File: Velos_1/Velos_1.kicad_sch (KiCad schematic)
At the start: 31 parts, among them J1 conector_motor, J2 S_Bus, J3 llave_habilitacion, J4 parada_emergencia, J5 V_in +9VDC, J6 Control Driver, K1 Relay_SPDT, Q1 BC548, Q2 BC548, Q3 BC548, Q4 BC548, Q5 BC548, U1 LM358, U2 L7805

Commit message: nano a mega y cambios en circuito atenuador
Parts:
- removed A1: Arduino_Nano_v2.x, Module:Arduino_Nano, symbol MCU_Module:Arduino_Nano_v2.x
- removed C2: 100nF, symbol Device:C
- removed R5: 33k, Resistor_THT:R_Axial_DIN0204_L3.6mm_D1.6mm_P5.08mm_Horizontal, symbol Device:R
- C1: value 100nF -> 100uF
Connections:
- net Ref vel_0 is gone; now on net Ref vel_D: RV1.2
- net +9V: now also A2.VIN
- net Analog_out: now also RV2.3; no longer RV2.1
- net Dir: now also A2.D5
- net Enable: now also A2.D6
- net GND: now also A2.GND6 (GND), U1.3 (+); no longer RV2.3
- net PWM: now also A2.D7
- net Puls: now also A2.D4
- net S-BUS: now also A2.D9
- net at C1.1, R4.2: now also RV2.1
- net at Q2.1 (C), R3.2: now also A2.D3 (D3_INT1)
- net at R1.2: now also A2.D2 (D2_INT0)
- net Ref vel_D: now reaches A2.A0
- no-connect marks 22 -> 78
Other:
- moved on the sheet: A2, C1, C3, C4, D1, J1, J2, J3, J4, J5, J6, K1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

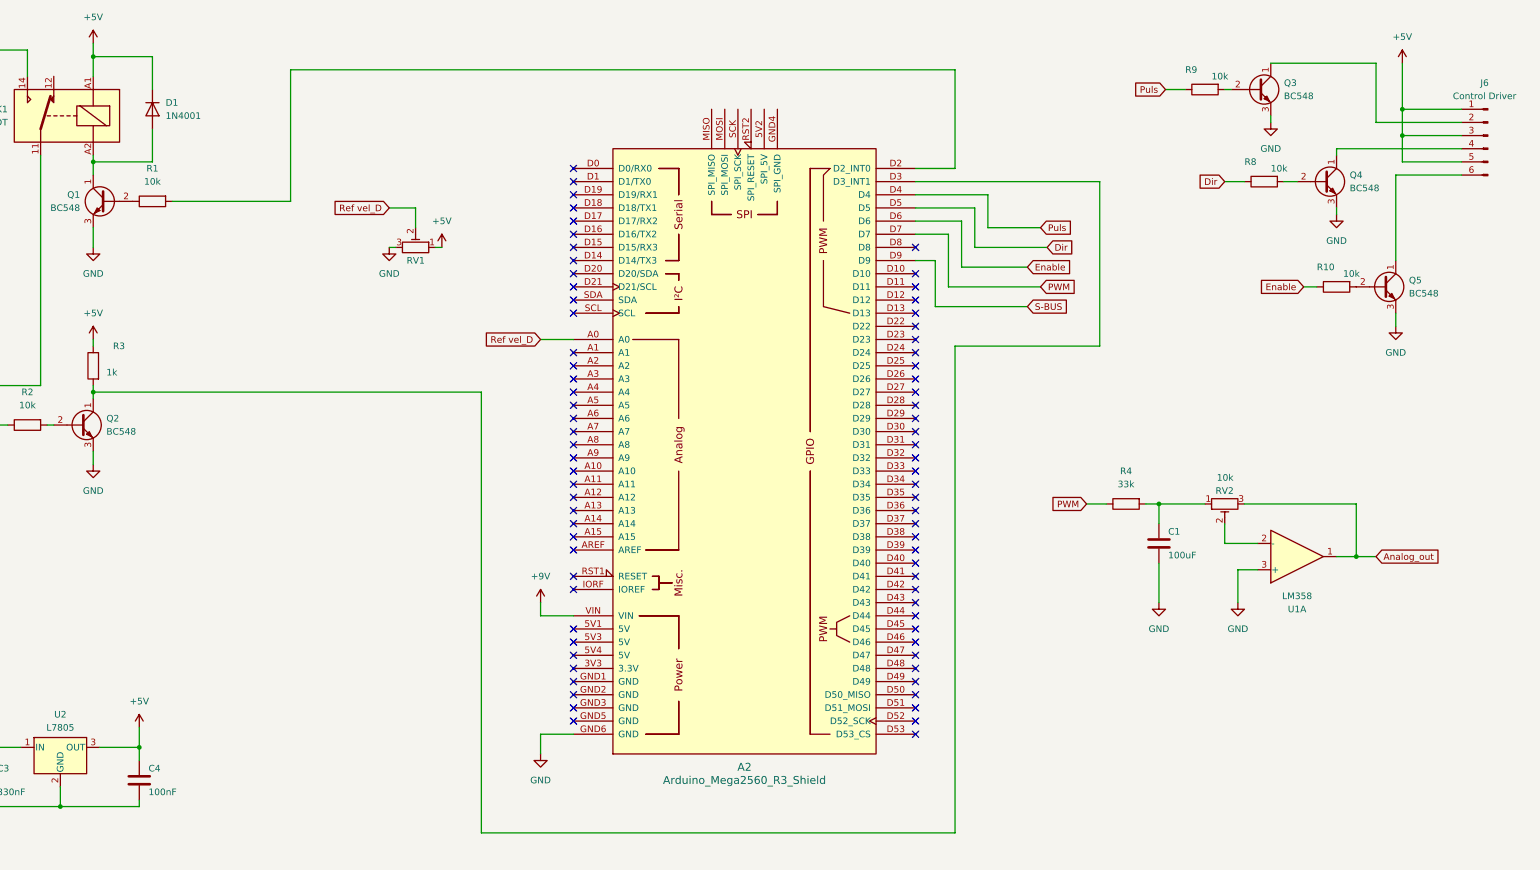
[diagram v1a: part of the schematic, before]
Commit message: componentes colocados pcb
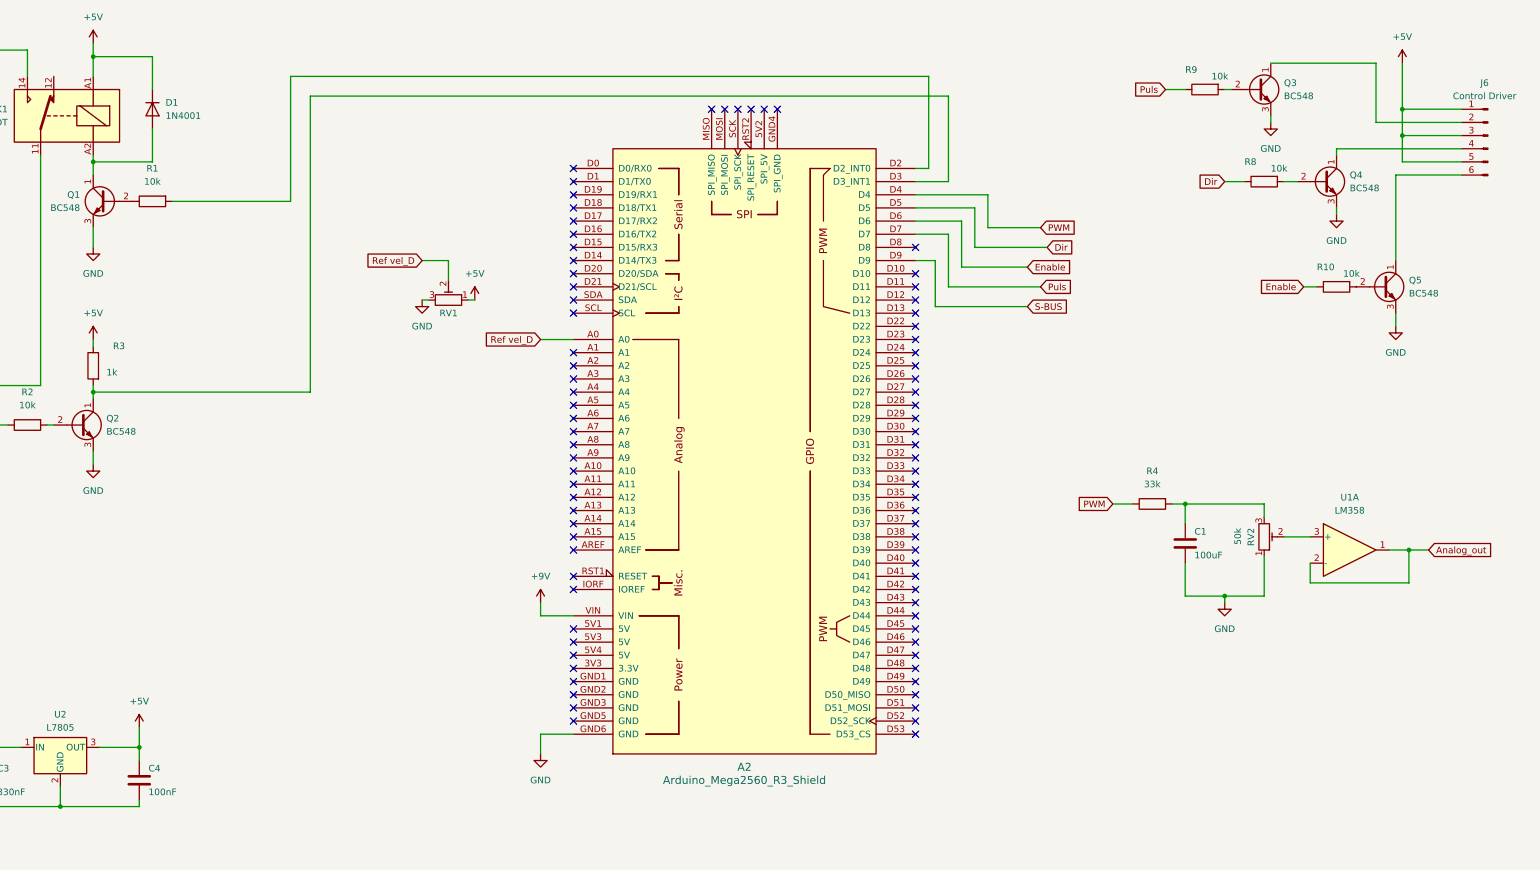
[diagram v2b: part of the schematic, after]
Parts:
- RV1: footprint Potentiometer_THT:Potentiometer_Bourns_3266Y_Vertical -> Potentiometer_THT:Potentiometer_Bourns_3009Y_Horizontal
- RV2: value 10k -> 50k; footprint Potentiometer_THT:Potentiometer_Bourns_3266Y_Vertical -> Potentiometer_THT:Potentiometer_Bourns_3009Y_Horizontal
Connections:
- net Analog_out: now also U1.2 (-); no longer RV2.3
- net GND: now also RV2.1; no longer U1.3 (+)
- net PWM: now also A2.D4; no longer A2.D7
- net Puls: now also A2.D7; no longer A2.D4
- net at C1.1, R4.2: now also RV2.3; no longer RV2.1
- net at RV2.2: now also U1.3 (+); no longer U1.2 (-)
- no-connect marks 78 -> 84
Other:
- moved on the sheet: C1, R4, RV1, RV2, U1A

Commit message: placa
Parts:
- removed J1: conector_motor, Connector_PinHeader_2.54mm:PinHeader_1x10_P2.54mm_Horizontal, symbol Connector:Conn_01x10_Pin
- removed RV1: R_Potentiometer_Trim, Potentiometer_THT:Potentiometer_Bourns_3009Y_Horizontal, symbol Device:R_Potentiometer_Trim
- removed RV2: 50k, Potentiometer_THT:Potentiometer_Bourns_3009Y_Horizontal, symbol Device:R_Potentiometer_Trim
- added C5: 100nF, Capacitor_THT:C_Disc_D5.0mm_W2.5mm_P5.00mm, symbol Device:C
- added J1: conector_motor, TerminalBlock_Phoenix:TerminalBlock_Phoenix_MKDS-1,5-7_1x07_P5.00mm_Horizontal, symbol Connector:Conn_01x07_Pin
- added J7: potenciometro, Connector_PinHeader_2.54mm:PinHeader_1x03_P2.54mm_Vertical, symbol Connector:Conn_01x03_Pin
- added unit 2 of U1
- added unit 3 of U1
- C1: footprint (none) -> Capacitor_THT:CP_Radial_D6.3mm_P2.50mm
- C3, C4: footprint (none) -> Capacitor_THT:C_Disc_D5.0mm_W2.5mm_P5.00mm
- J2: footprint Connector_PinHeader_2.54mm:PinHeader_1x02_P2.54mm_Horizontal -> Connector_PinHeader_2.54mm:PinHeader_1x02_P2.54mm_Vertical
- J3, J4, J5: footprint Connector_PinHeader_2.54mm:PinHeader_1x02_P2.54mm_Horizontal -> TerminalBlock_Phoenix:TerminalBlock_Phoenix_MKDS-1,5-2_1x02_P5.00mm_Horizontal
- J6: footprint Connector_PinHeader_2.54mm:PinHeader_1x06_P2.54mm_Vertical -> TerminalBlock_Phoenix:TerminalBlock_Phoenix_MKDS-1,5-6_1x06_P5.00mm_Horizontal
- K1: footprint Relay_THT:Relay_SPDT_SANYOU_SRD_Series_Form_C -> Relay_THT:Relay_SPDT_Hongfa_JQC-3FF_0XX-1Z
- R1, R10, R2, R3, R8, R9: footprint Resistor_THT:R_Axial_DIN0204_L3.6mm_D1.6mm_P5.08mm_Horizontal -> Resistor_THT:R_Axial_DIN0204_L3.6mm_D1.6mm_P7.62mm_Horizontal
- R4: value 33k -> 47k; footprint Resistor_THT:R_Axial_DIN0204_L3.6mm_D1.6mm_P5.08mm_Horizontal -> Resistor_THT:R_Axial_DIN0204_L3.6mm_D1.6mm_P7.62mm_Horizontal
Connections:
- net +5V: now also A2.5V1 (5V), A2.5V3 (5V), A2.5V4 (5V), J6.2 (Pin_2), J7.1 (Pin_1), U1.8 (V+); no longer J6.3 (Pin_3)
- net +9V: now also J5.2 (Pin_2); no longer J5.1 (Pin_1)
- net Analog_out: now also C5.1, J1.4 (Pin_4)
- net GND: now also A2.GND1 (GND), A2.GND3 (GND), J2.1 (Pin_1), J4.1 (Pin_1), J5.1 (Pin_1), C5.2, J1.6 (Pin_6), J1.7 (Pin_7), J7.3 (Pin_3), U1.4 (V-); no longer A2.GND6 (GND), J2.2 (Pin_2), J4.2 (Pin_2), J5.2 (Pin_2)
- net S-BUS: now also A2.D15 (D15/RX3), J2.2 (Pin_2); no longer A2.D9, J2.1 (Pin_1)
- net Seguridad: now also J4.2 (Pin_2), J1.2 (Pin_2); no longer J4.1 (Pin_1)
- net V_Ctrl: now also J1.5 (Pin_5)
- net at Q3.1 (C): now also J6.3 (Pin_3); no longer J6.2 (Pin_2)
- net at U1.3 (+): now also C1.1, R4.2
- net at K1.11: now also J1.3 (Pin_3)
- net at A2.A8: now also J7.2 (Pin_2)
- net Power on renamed Power_on_relay
- net Power_on_relay: no longer J3.2 (Pin_2)
- net Ref vel_D: no longer names the net of A2.A0
- new net Power_on_motor: J1.1 (Pin_1), J3.2 (Pin_2)
- no-connect marks 84 -> 81
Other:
- moved on the sheet: C1, C3, C4, D1, J2, J3, J4, J5, J6, K1, Q1, Q2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

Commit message: placa final
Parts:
- added J8: Control Driver_backup, Connector_PinHeader_2.54mm:PinHeader_1x06_P2.54mm_Vertical, symbol Connector:Conn_01x06_Pin
- added J9: Conn_01x01_Pin, Connector_PinHeader_2.54mm:PinHeader_1x01_P2.54mm_Vertical, symbol Connector:Conn_01x01_Pin
- C1: value 100uF -> 22uF
- R4: value 47k -> 10k
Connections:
- net +5V: now also J8.1 (Pin_1)
- net GND: now also A2.GND2 (GND), J8.2 (Pin_2), J9.1 (Pin_1)
- net A0: now reaches A2.A0
- net A0: now also J8.3 (Pin_3)
- net A1: now reaches A2.A1
- net A1: now also J8.4 (Pin_4)
- net A2: now reaches A2.A2
- net A2: now also J8.5 (Pin_5)
- net A3: now reaches A2.A3
- net A3: now also J8.6 (Pin_6)
- no-connect marks 81 -> 76
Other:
- moved on the sheet: C1, R4, U1A, U1B, U1C
